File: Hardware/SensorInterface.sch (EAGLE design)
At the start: 69 parts, among them J3 CONN_32.54_SCREW, J4 CONN_32.54_SCREW, J5 CONN_42.54_SCREW, Q1 DMG3404, Q2 DMG3404, Q3 DMG3404, Q4 DMG3404, Q5 DMG3404, U10 SN74AHC1G86DCK, U11 MCP6041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

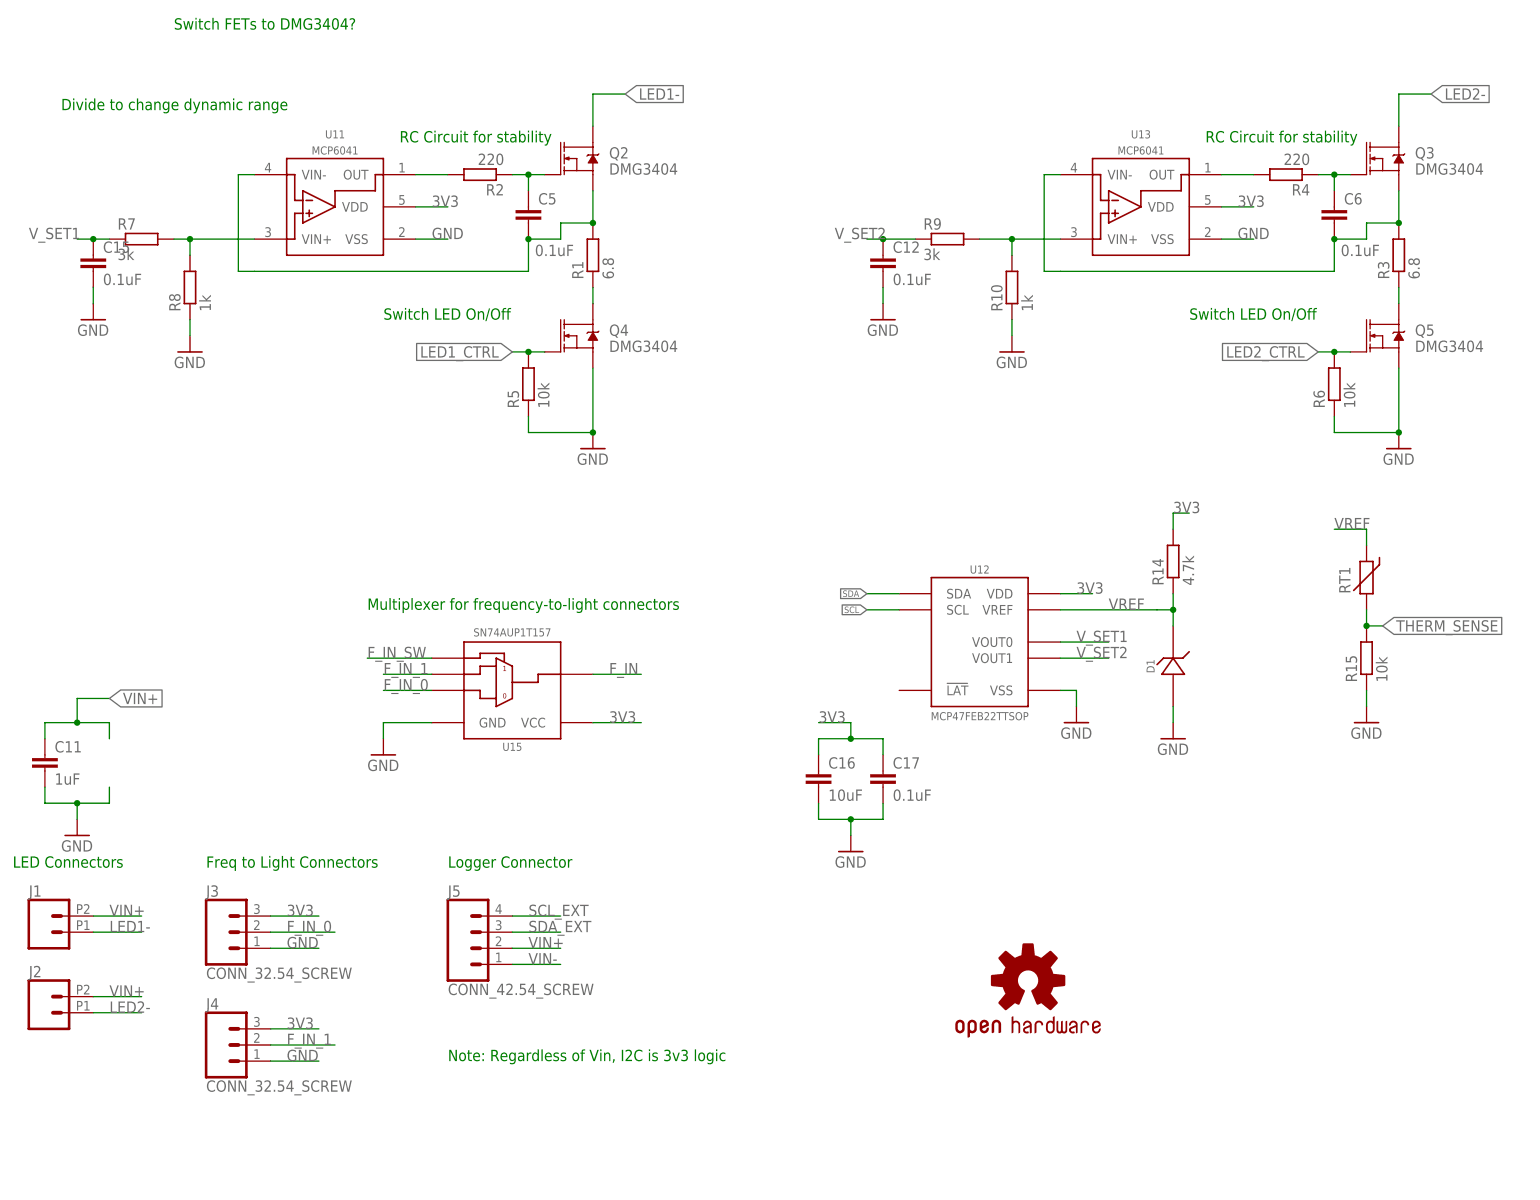
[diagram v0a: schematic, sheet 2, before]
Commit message: Continued layout update
Layout is functional for v0.1, review and clean up still required but functional layout completed
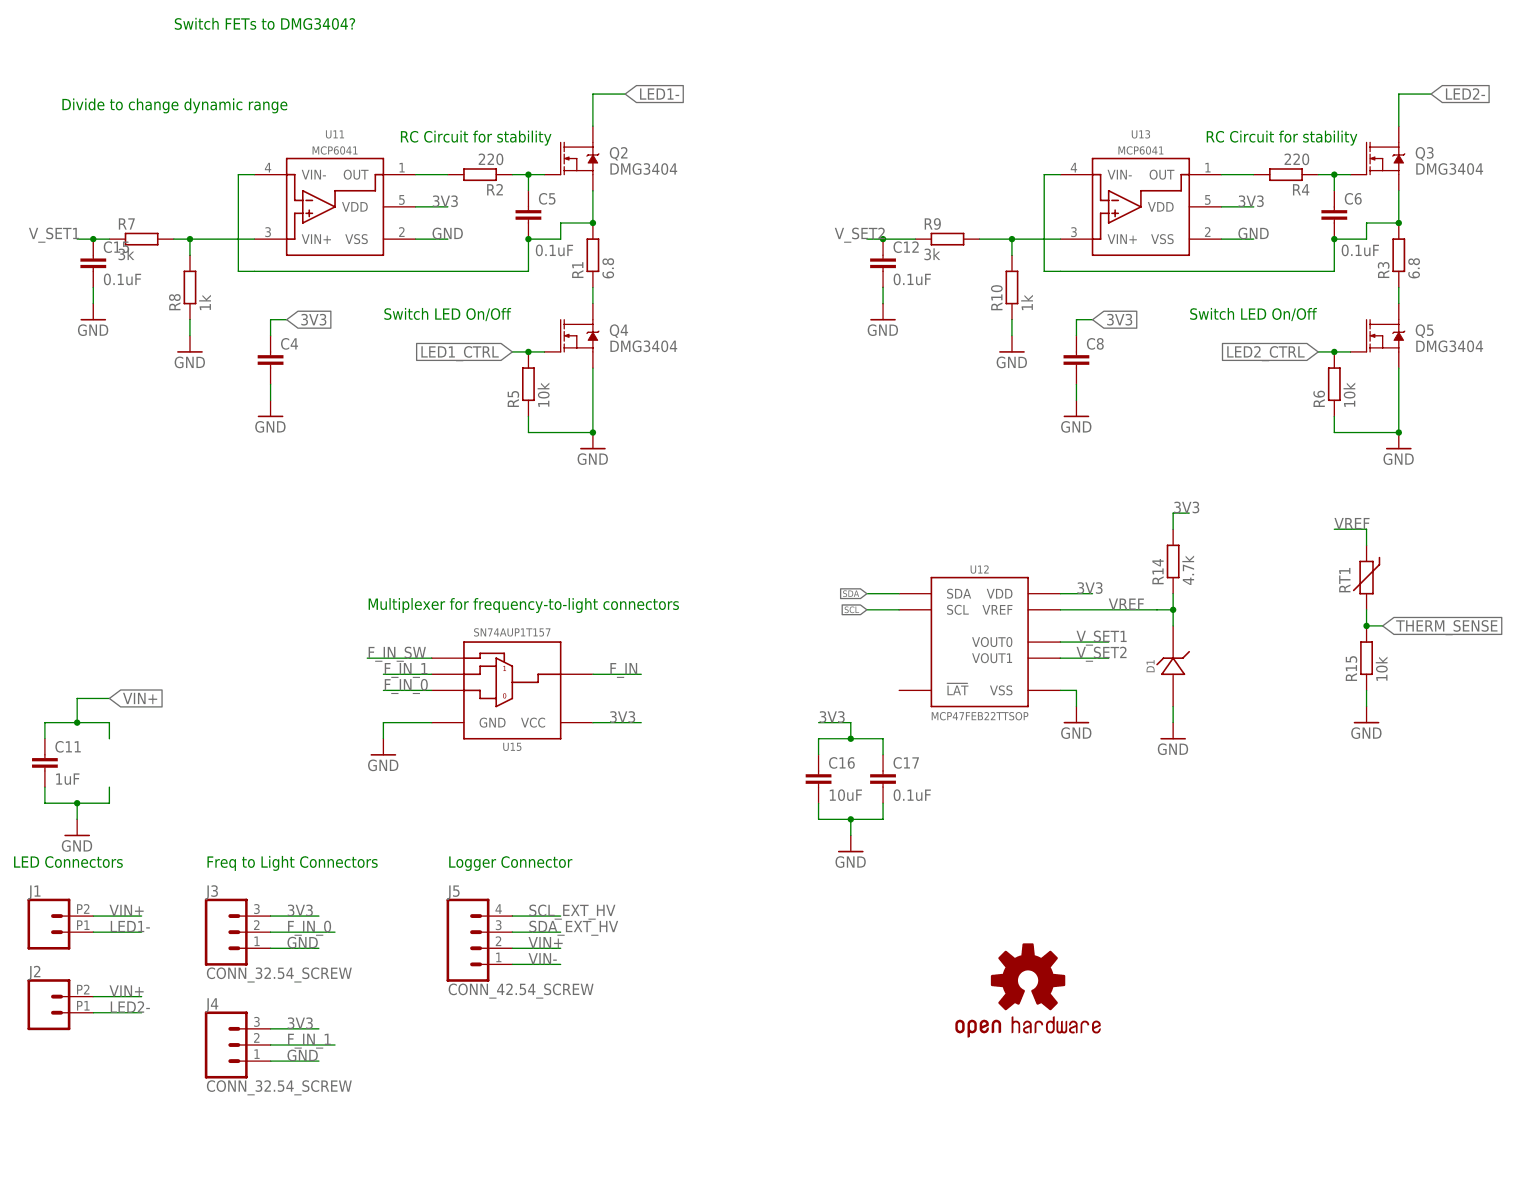
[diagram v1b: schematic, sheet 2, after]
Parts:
- added C4, C8: (no value), bschulz_passives:C-EU0.1UFC0402
- C3: device bschulz_passives:C-EUC0603 -> bschulz_passives:C-EU0.1UFC0402
- R11, R12, R13: device bschulz_passives:R-EU_R0603 -> bschulz_passives:R-EU_10KR0402
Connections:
- new net SCL_EXT_HV: J5.4, U16.B1
- new net SDA_EXT_HV: J5.3, U16.B2
- net 3V3: now also C4.1, C8.1
- net GND: now also C4.2, C8.2
- net SCL: no longer U16.A1
- net SCL_EXT: now also U16.A1; no longer J5.4, U16.B1
- net SDA: no longer U16.A2
- net SDA_EXT: now also U16.A2; no longer J5.3, U16.B2
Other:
- note removed: "Note: Regardless of Vin, I2C is 3v3 logic"

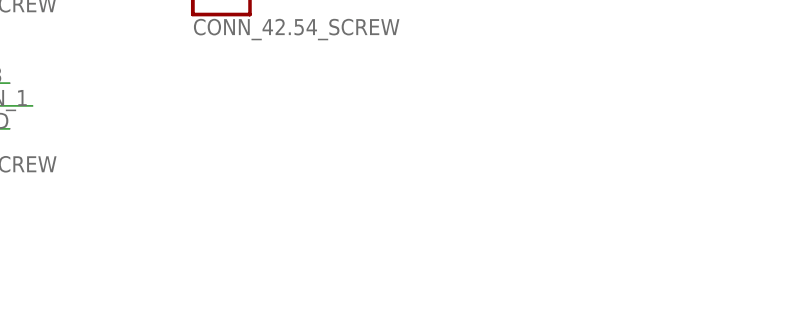
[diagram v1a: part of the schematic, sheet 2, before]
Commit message: Added mount holes, cleaned up sim
Cleaned up simulation files and gitignore, added mounting holes to board
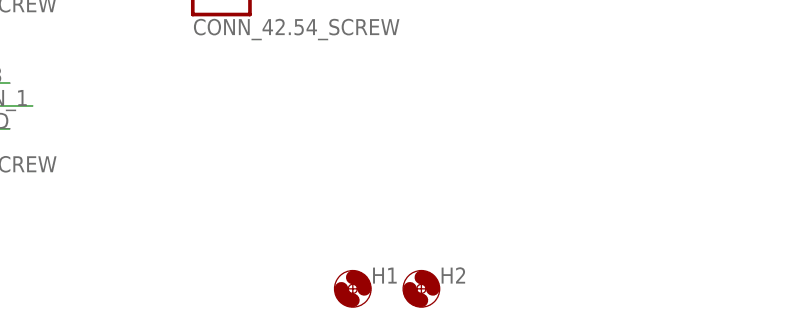
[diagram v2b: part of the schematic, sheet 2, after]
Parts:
- added H1, H2: (no value), bschulz:MOUNTING_HOLE2_NP
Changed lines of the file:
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@@
 <part name="C8" library="bschulz_passives" deviceset="C-EU" device="C0402" technology="0.1UF"/>
 <part name="GND22" library="supply1" library_urn="urn:adsk.eagle:library:371" deviceset="GND" device=""/>
+<part name="H1" library="bschulz" deviceset="MOUNTING_HOLE" device="2_NP"/>
+<part name="H2" library="bschulz" deviceset="MOUNTING_HOLE" device="2_NP"/>
 </parts>
 <sheets>
@@
 <attribute name="VALUE" x="190.5" y="137.16" size="1.778" layer="96"/>
 </instance>
+<instance part="H1" gate="G$1" x="111.76" y="20.32" smashed="yes">
+<attribute name="NAME" x="113.792" y="20.9042" size="1.778" layer="95"/>
+<attribute name="VALUE" x="113.792" y="17.8562" size="1.778" layer="96"/>
+</instance>
+<instance part="H2" gate="G$1" x="119.38" y="20.32" smashed="yes">
+<attribute name="NAME" x="121.412" y="20.9042" size="1.778" layer="95"/>
+<attribute name="VALUE" x="121.412" y="17.8562" size="1.778" layer="96"/>
+</instance>
 </instances>
